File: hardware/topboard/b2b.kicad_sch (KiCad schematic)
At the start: 32 parts

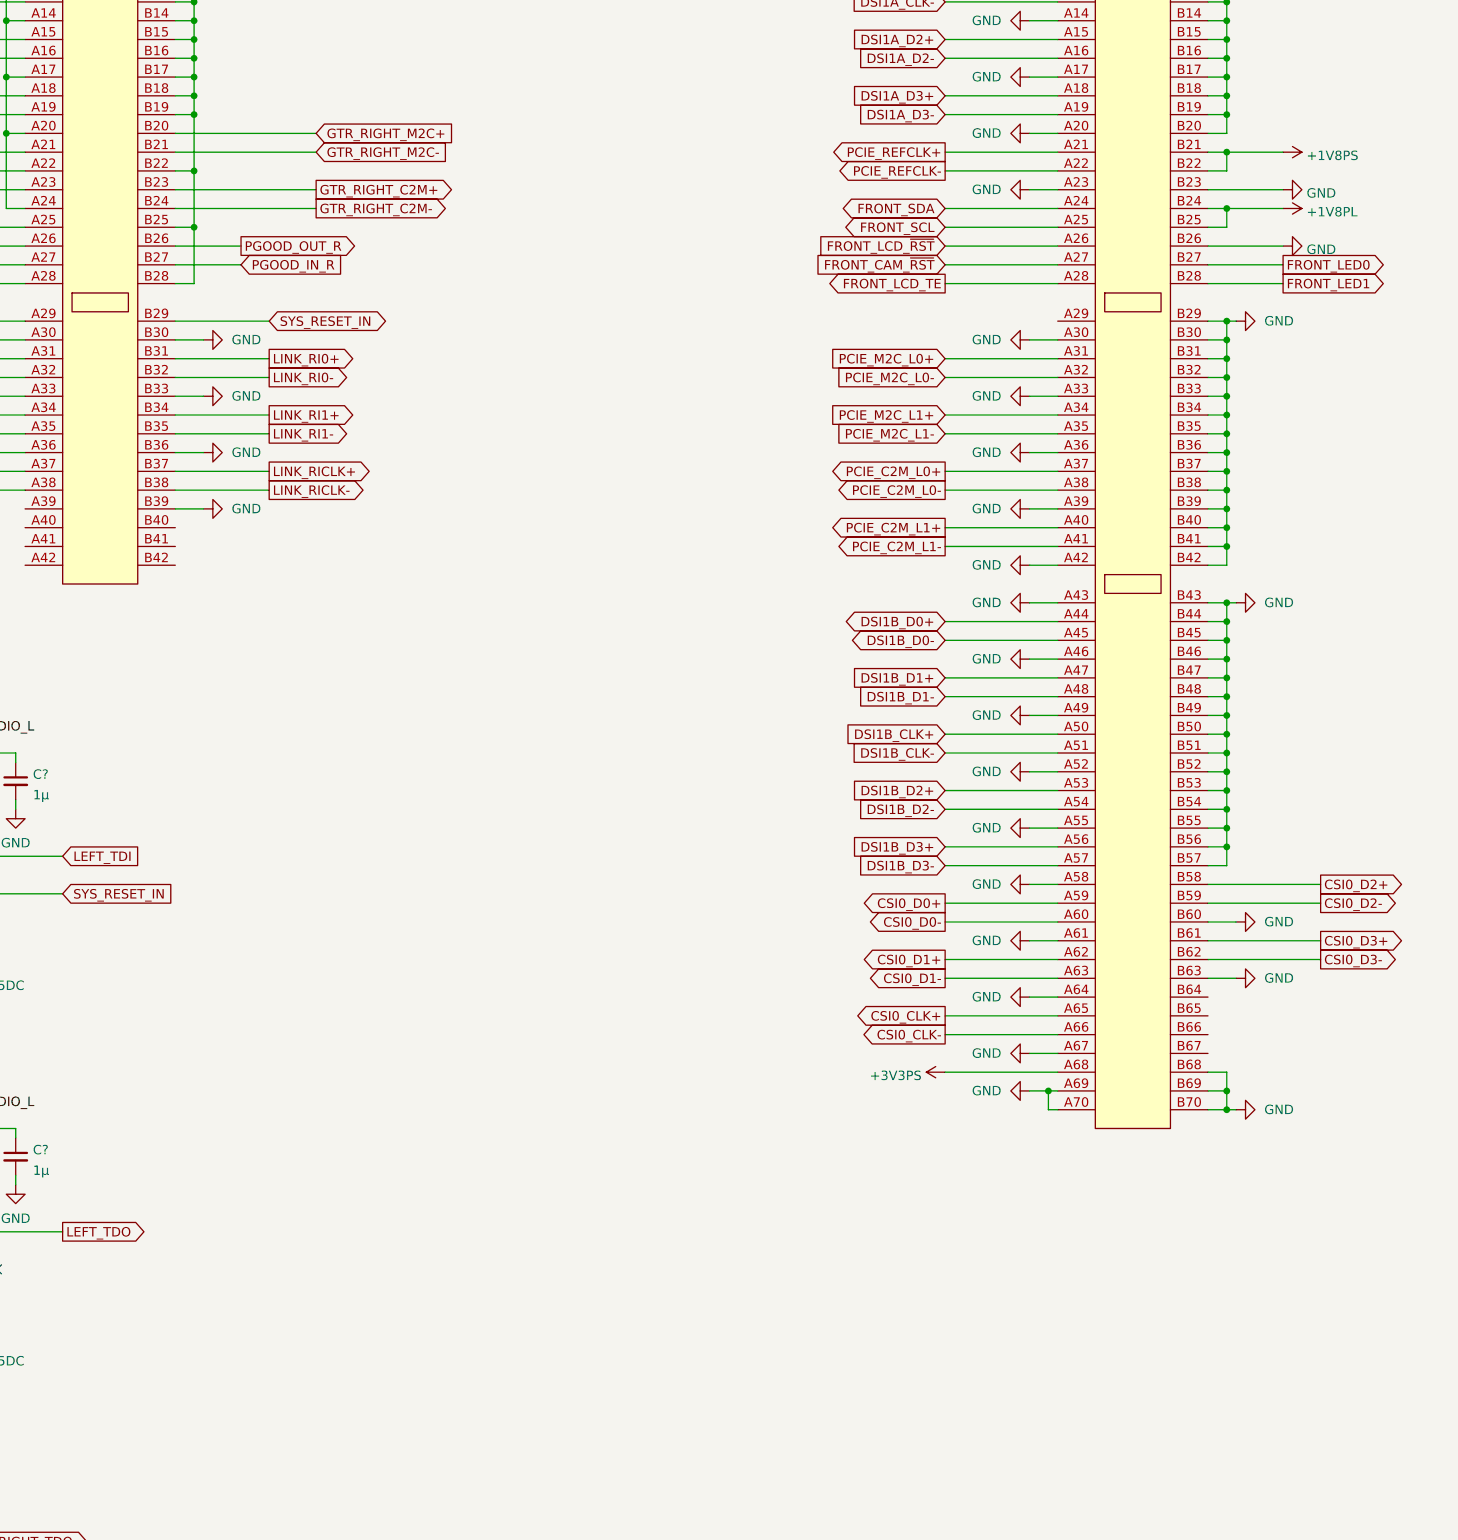
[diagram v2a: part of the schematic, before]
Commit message: Add PCIe and camera to front board
Signed-off-by: gatecat <gatecat@ds0.me>
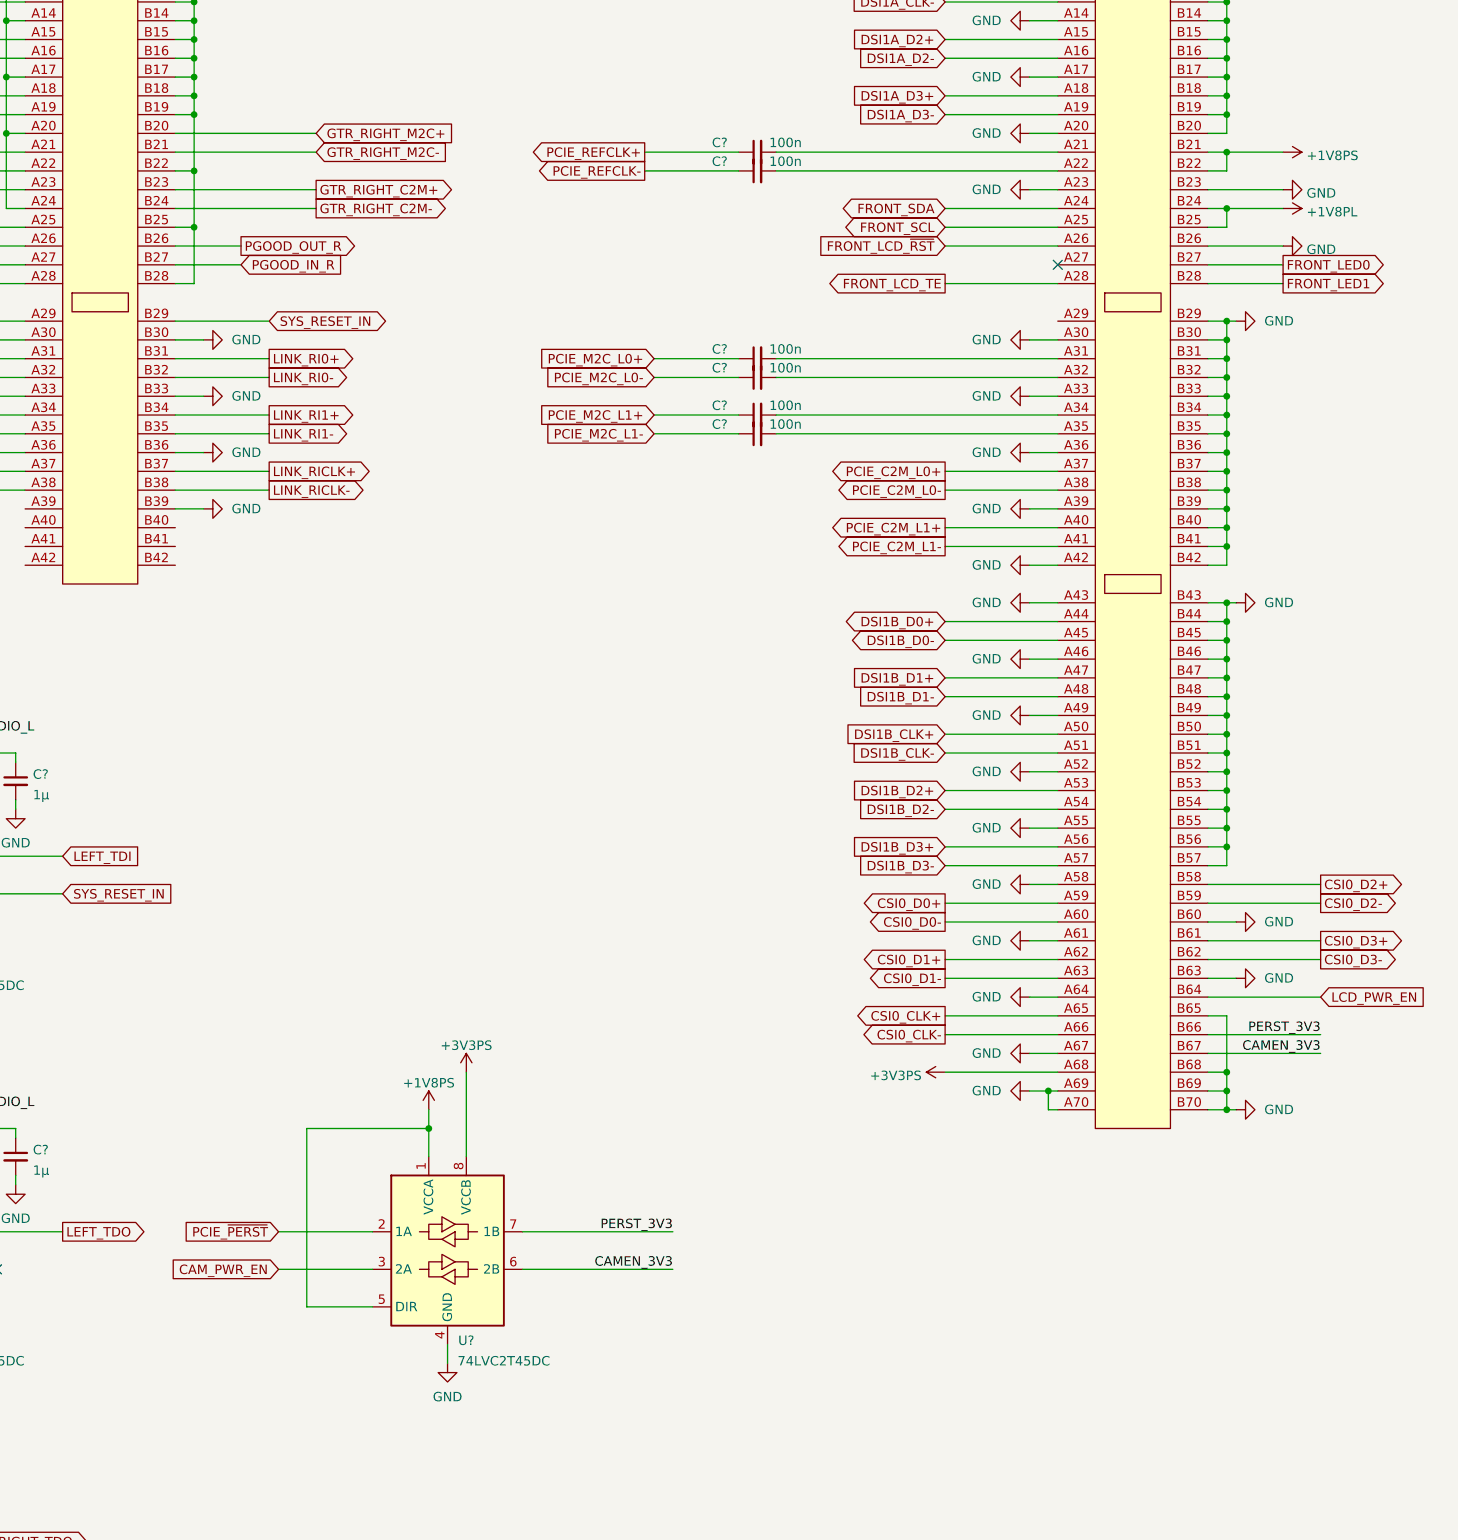
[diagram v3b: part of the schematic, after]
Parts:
- added C? (x6): 100n, symbol Device:C_Small
- added U?: 74LVC2T45DC, Package_SO:VSSOP-8_2.3x2mm_P0.5mm, symbol Logic_LevelTranslator:74LVC2T45DC
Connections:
- net +1V8PS: now also U?.1 (VCCA), U?.5 (DIR)
- net +3V3PS: now also U?.8 (VCCB)
- net GND: now also J?.B65, U?.4 (GND)
- net PCIE_M2C_L0+: now also C?.1; no longer J?.A31
- net PCIE_M2C_L0-: now also C?.1; no longer J?.A32
- net PCIE_M2C_L1+: now also C?.1; no longer J?.A34
- net PCIE_M2C_L1-: now also C?.1; no longer J?.A35
- net PCIE_REFCLK+: now also C?.1; no longer J?.A21
- net PCIE_REFCLK-: now also C?.1; no longer J?.A22
- net LCD_PWR_EN: now reaches J?.B64
- net PERST_3V3: now reaches J?.B66
- net PERST_3V3: now also U?.7 (1B)
- net CAMEN_3V3: now reaches J?.B67
- net CAMEN_3V3: now also U?.6 (2B)
- net FRONT_CAM_~{RST}: no longer names the net of J?.A27
- new net: C?.2, J?.A31
- new net: C?.2, J?.A32
- new net: C?.2, J?.A35
- new net: C?.2, J?.A21
- new net: C?.2, J?.A22
- new net: C?.2, J?.A34
- new net CAM_PWR_EN: U?.3 (2A)
- new net PCIE_~{PERST}: U?.2 (1A)
- no-connect marks 3 -> 4

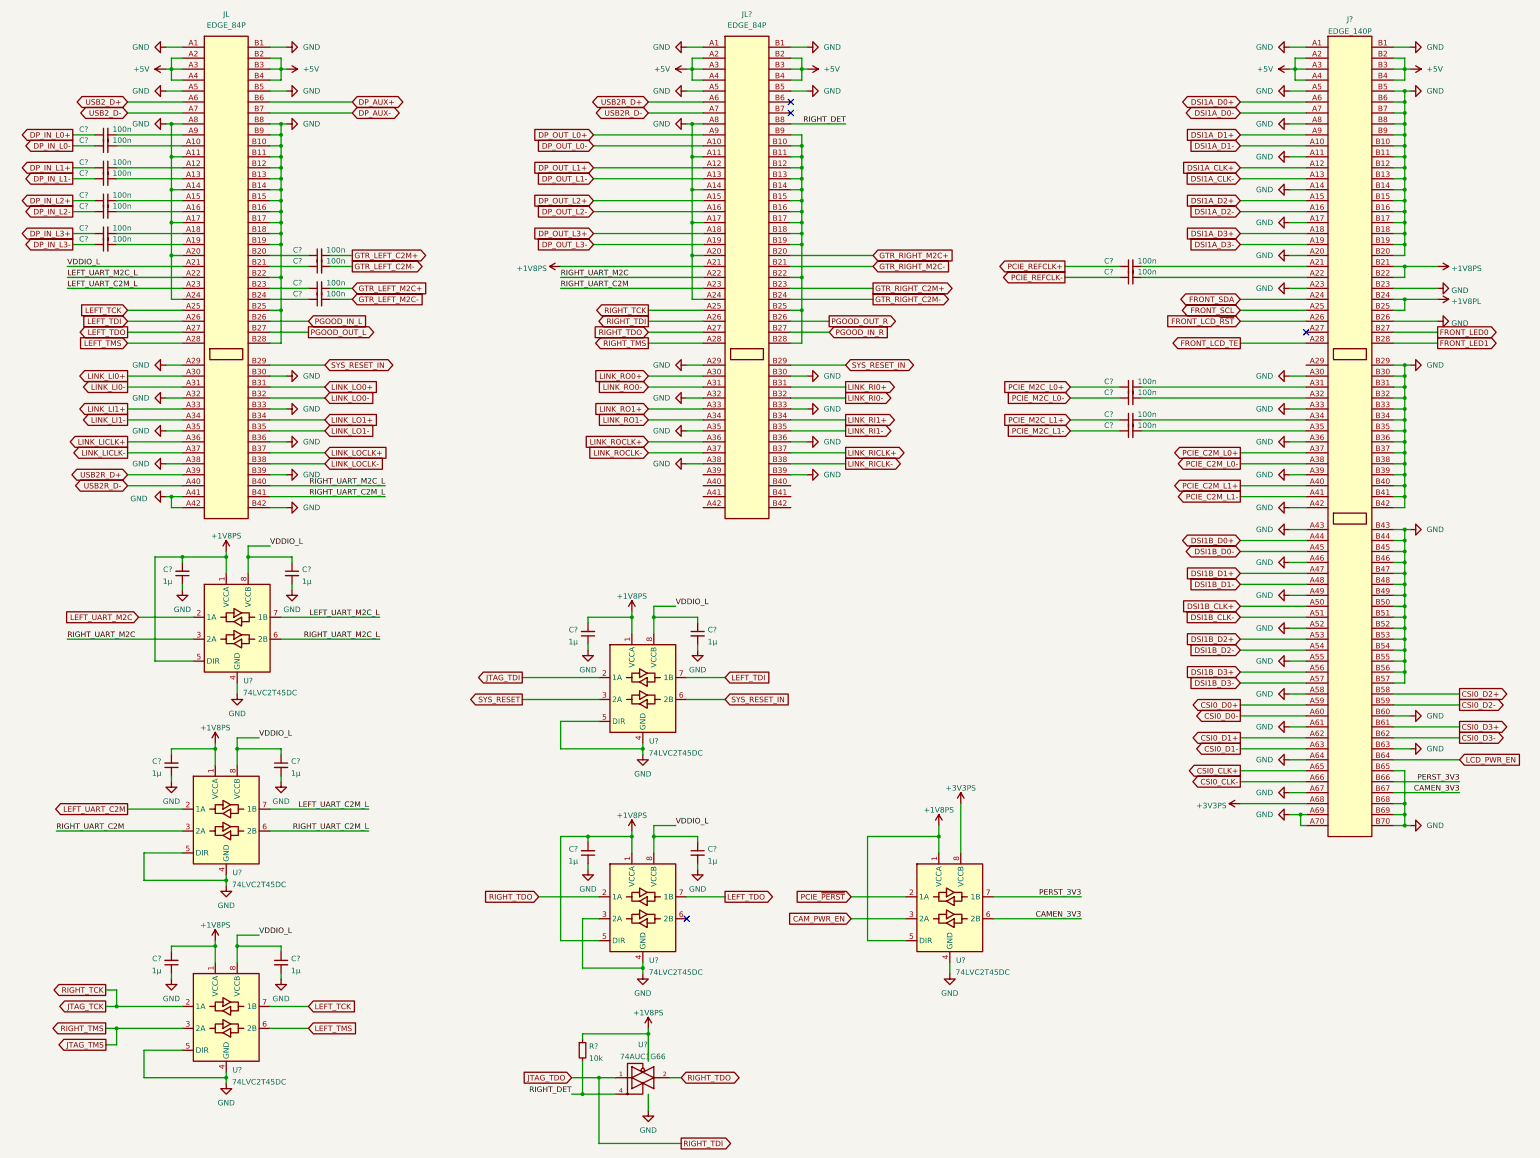
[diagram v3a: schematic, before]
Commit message: Add some general control IO
Signed-off-by: gatecat <gatecat@ds0.me>
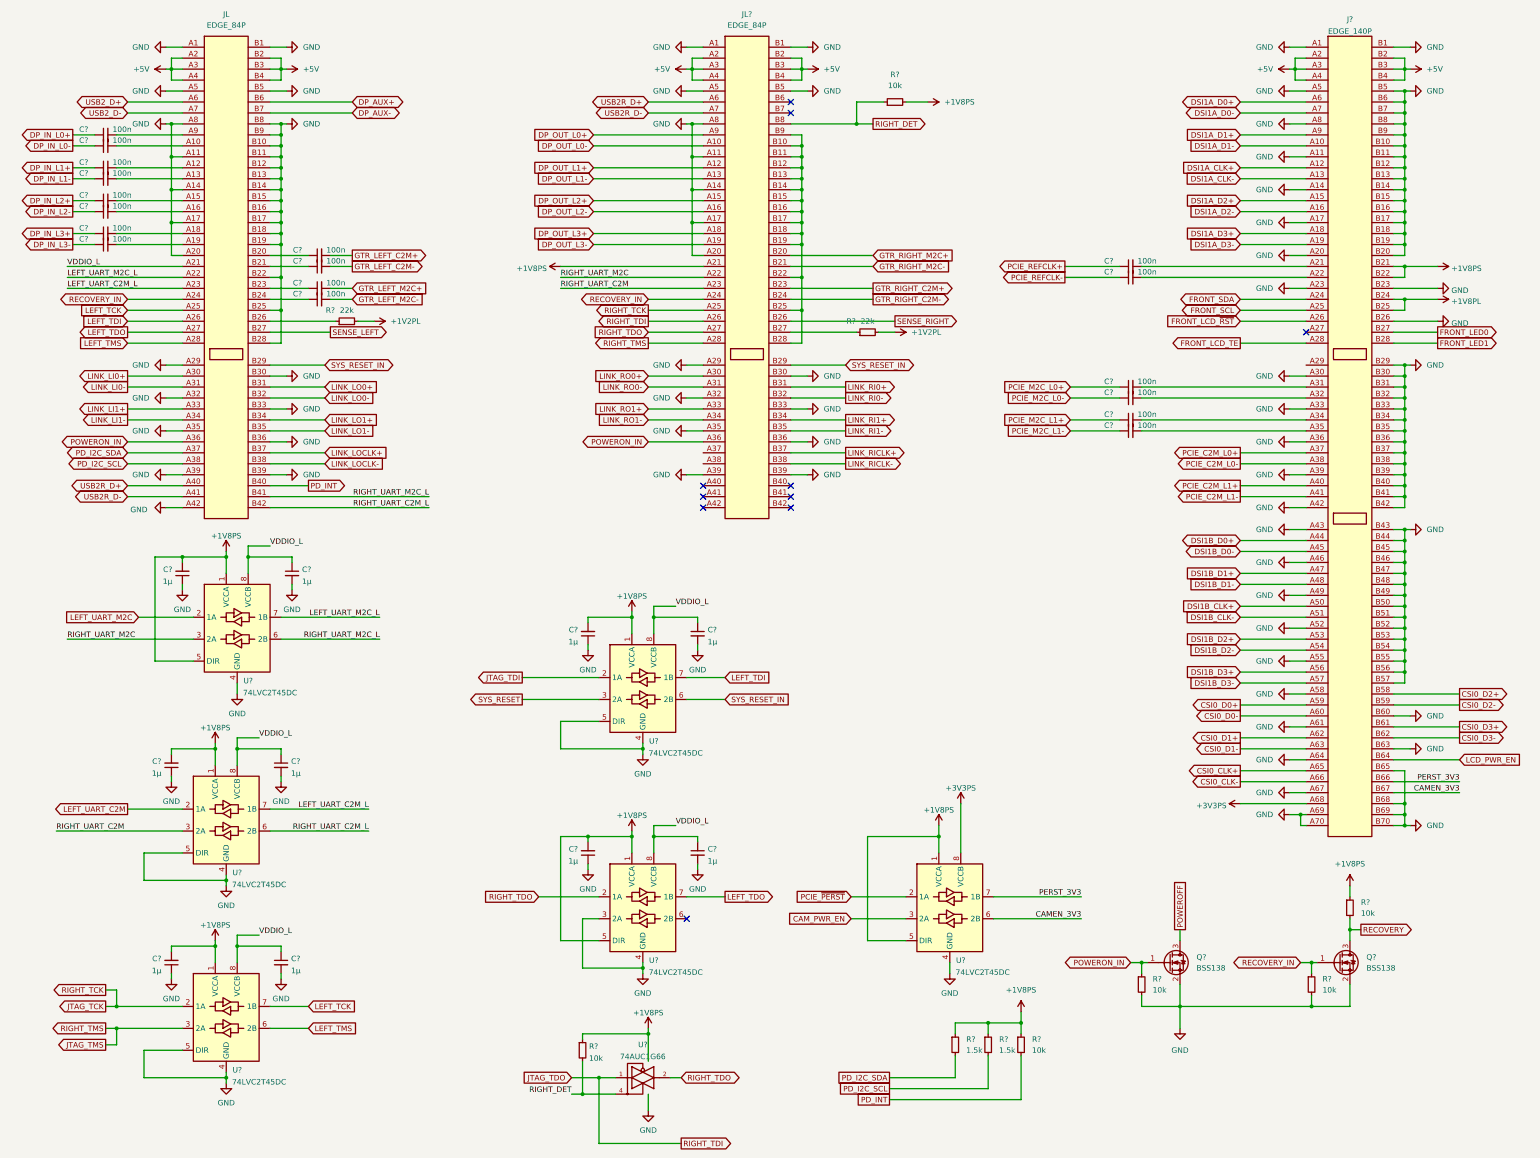
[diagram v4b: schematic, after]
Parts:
- added Q? (x2): BSS138, Package_TO_SOT_SMD:SOT-23, symbol Transistor_FET:BSS138
- added R? (x2): 1.5k, symbol Device:R_Small
- added R? (x2): 22k, symbol Device:R_Small
- added R? (x5): 10k, symbol Device:R_Small
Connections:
- net LINK_ROCLK+ is gone; now on net POWERON_IN: JL?.A36
- net +1V8PS: now also R?.1, R?.1, R?.1, R?.1, R?.2
- net GND: now also JL.A39, JL?.A39, Q?.2 (S), Q?.2 (S), R?.2, R?.2; no longer JL.A24, JL.A38, JL.A41, JL.B42, JL?.A24, JL?.A38
- net RIGHT_DET: now also R?.1
- net RIGHT_UART_C2M_L: now also JL.B42; no longer JL.B41
- net RIGHT_UART_M2C_L: now also JL.B41; no longer JL.B40
- net USB2R_D+: now also JL.A40; no longer JL.A39
- net USB2R_D-: now also JL.A41; no longer JL.A40
- net LINK_LICLK+ renamed POWERON_IN
- net POWERON_IN: now also Q?.1 (G), R?.1
- net LINK_LICLK- renamed PD_I2C_SDA
- net PD_I2C_SDA: now also R?.2
- net LINK_ROCLK-: no longer names the net of JL?.A37
- net PGOOD_IN_L: no longer names the net of JL.B26
- net PGOOD_IN_L: now also R?.1
- net PGOOD_IN_R: no longer names the net of JL?.B27
- net PGOOD_IN_R: now also R?.1
- net PGOOD_OUT_L renamed SENSE_LEFT
- net PGOOD_OUT_R renamed SENSE_RIGHT
- new net +1V2PL: R?.2, R?.2
- new net PD_I2C_SCL: JL.A38, R?.2
- new net PD_INT: JL.B40, R?.2
- new net POWEROFF: Q?.3 (D)
- new net RECOVERY: Q?.3 (D), R?.2
- new net RECOVERY_IN: JL.A24, JL?.A24, Q?.1 (G), R?.1
- no-connect marks 4 -> 10
